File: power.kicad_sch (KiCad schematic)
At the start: 60 parts, among them U10 MAX4495AAUT, U11 MAX4495AAUT, U4 TPSM828302ARDSR, U5 LP3962EMP-3.3/NOPB, U6 STWD100NYWY3F, U7 MAX4495AAUT, U8 MP5073GG-P, U9 MAX4495AAUT

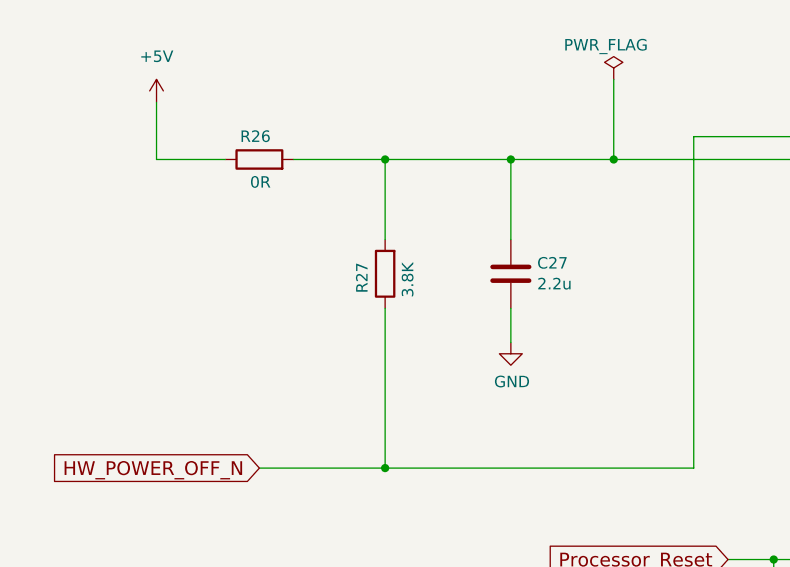
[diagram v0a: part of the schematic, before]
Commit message: Change a resistor, add a bunch of ground vias
Signed-off-by: Corey Minyard <corey@minyard.net>
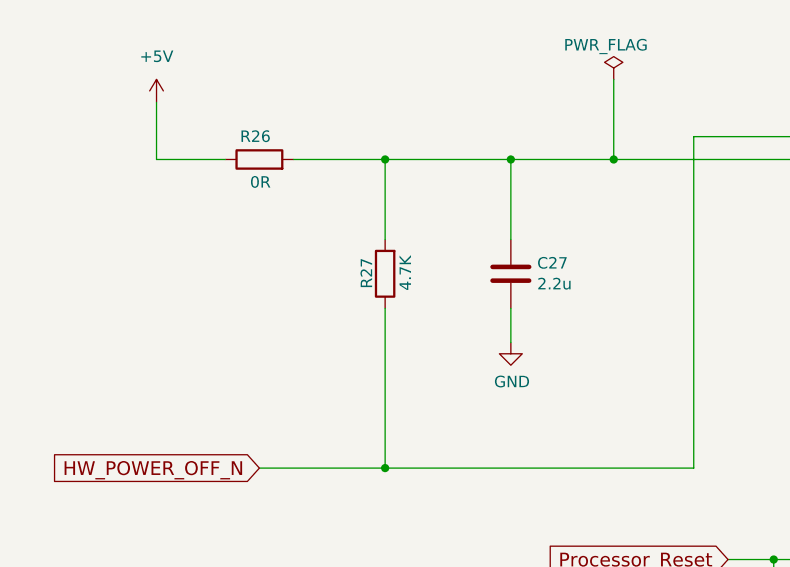
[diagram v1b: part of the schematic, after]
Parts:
- R27: value 3.8K -> 4.7K
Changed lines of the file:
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@@
 		(dnp no)
 		(property "Reference" "R27"
-			(at 63.5 104.14 90)
+			(at 64.008 103.632 90)
 			(effects
 				(font
@@
 			)
 		)
-		(property "Value" "3.8K"
-			(at 68.58 104.14 90)
+		(property "Value" "4.7K"
+			(at 68.326 103.378 90)
 			(effects
 				(font

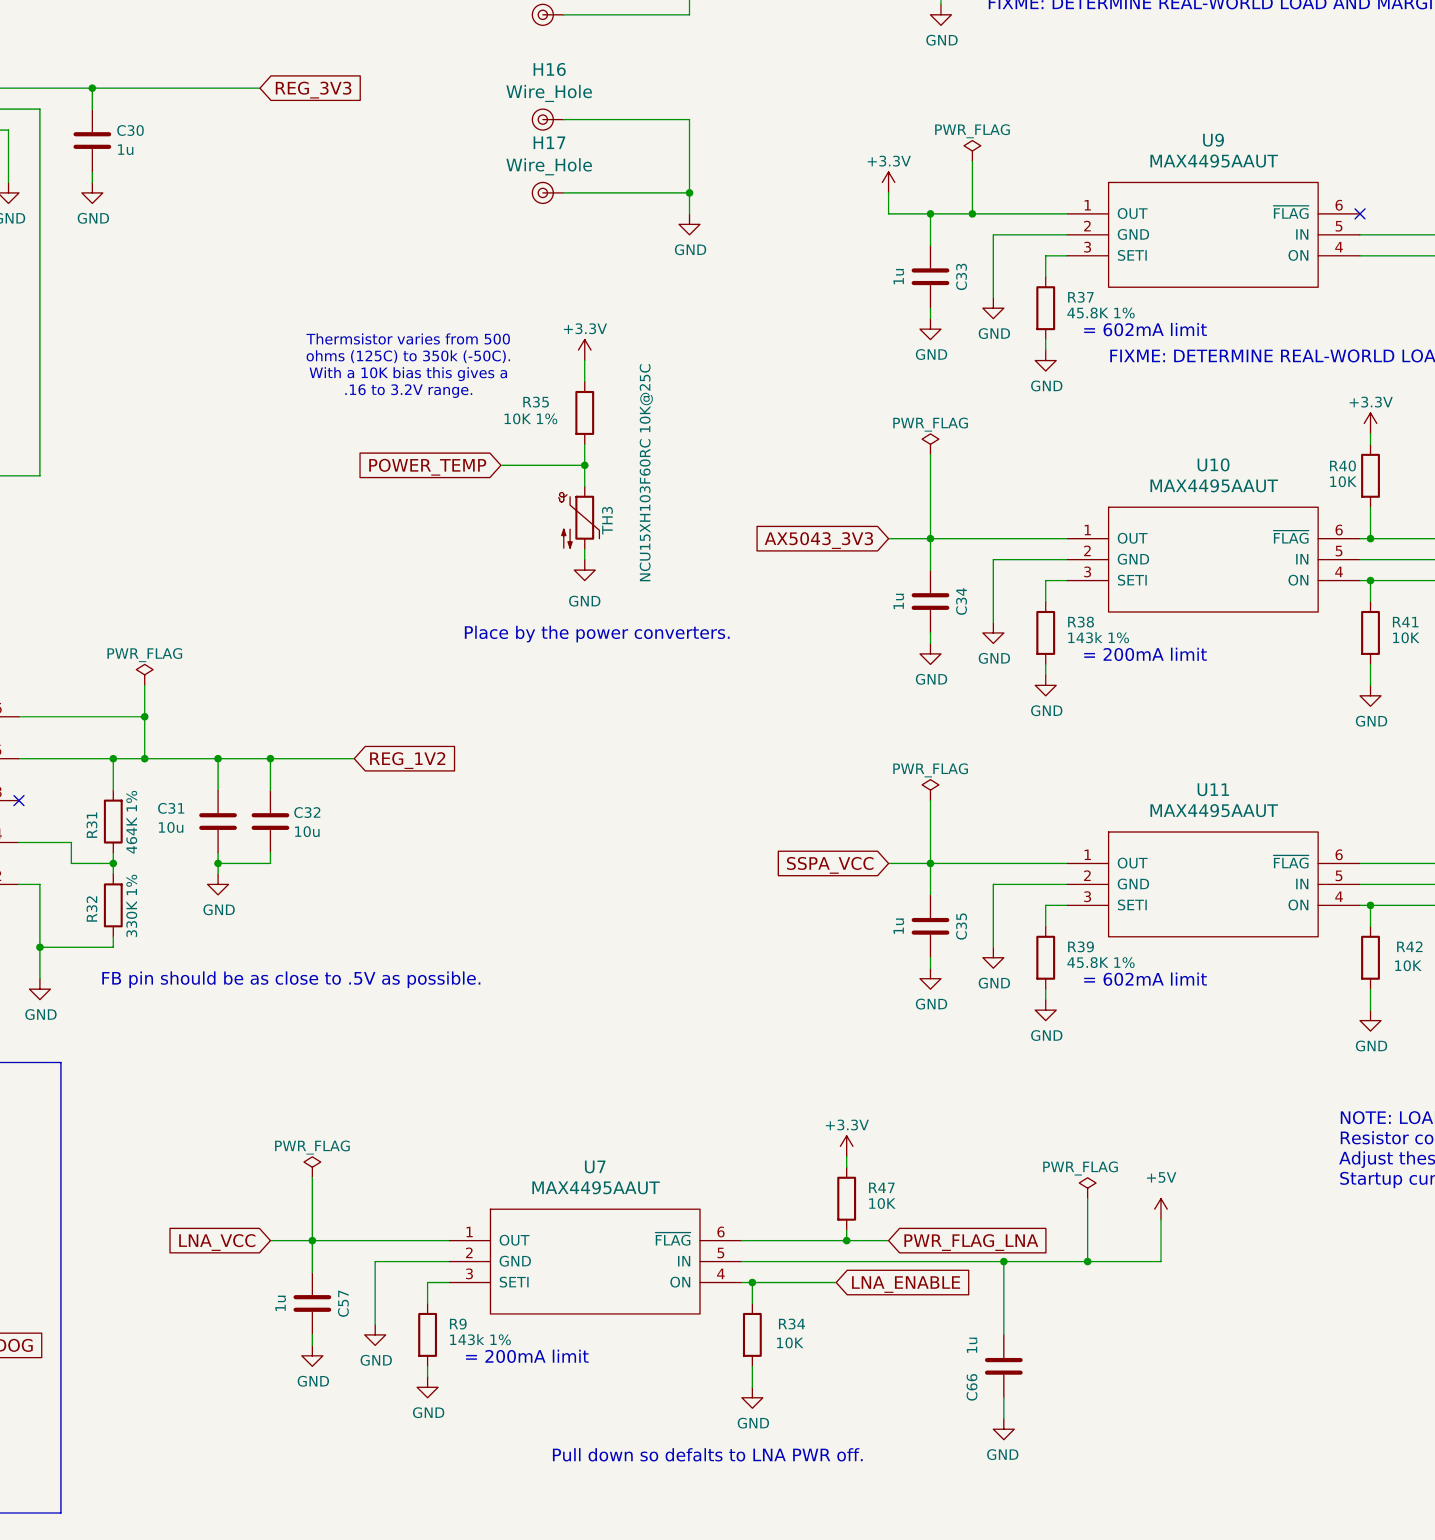
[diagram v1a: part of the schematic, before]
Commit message: Add a current limiter for on-board +5V devices
Signed-off-by: Corey Minyard <corey@minyard.net>
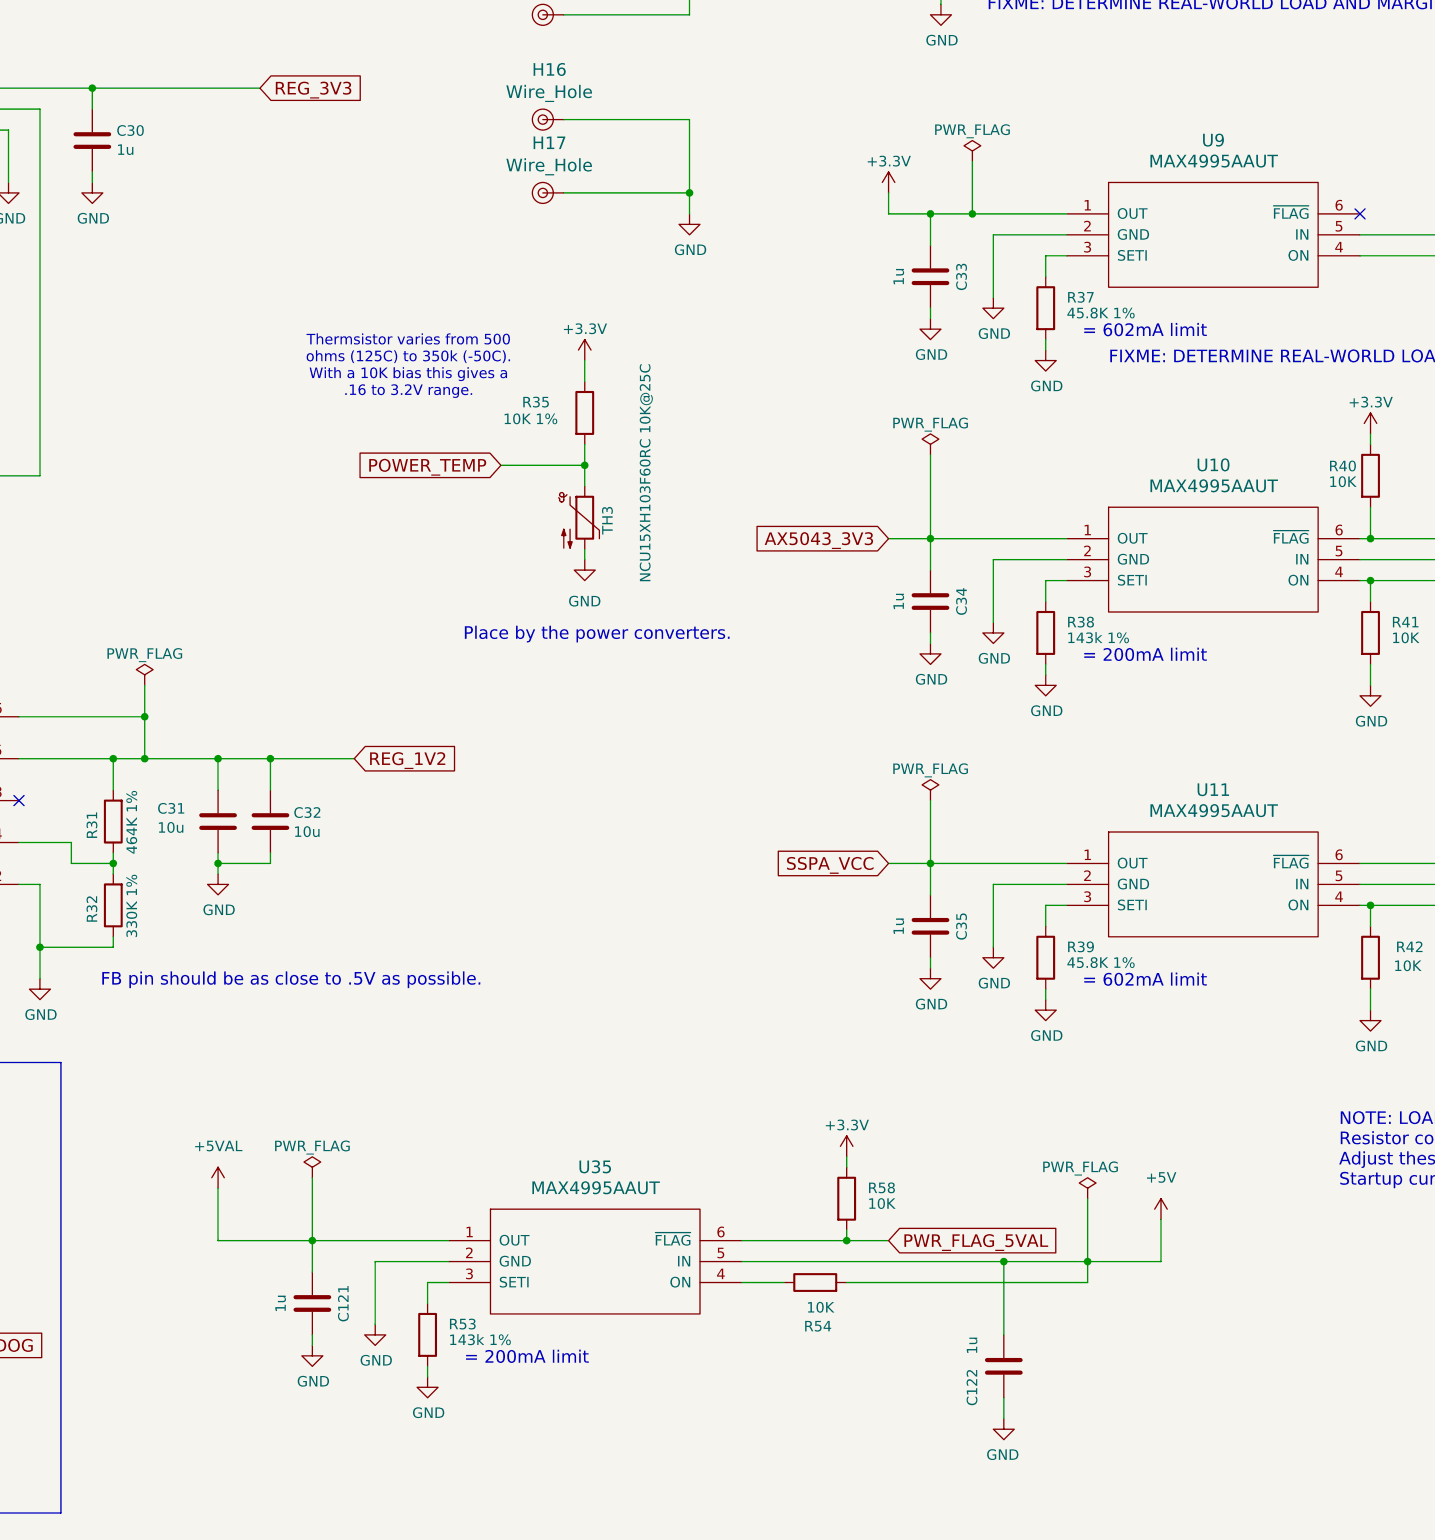
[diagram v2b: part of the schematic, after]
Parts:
- removed C57, C66: 1u, Capacitor_SMD:C_0805_2012Metric_Pad1.18x1.45mm_HandSolder, symbol Device:C
- removed R34, R47: 10K, Resistor_SMD:R_0603_1608Metric_Pad0.98x0.95mm_HandSolder, symbol Device:R
- removed R9: 143k 1%, Resistor_SMD:R_0603_1608Metric_Pad0.98x0.95mm_HandSolder, symbol Device:R
- removed U7: MAX4495AAUT, Package_TO_SOT_SMD:SOT-23-6_Handsoldering, symbol PACSAT_ICs:MAX4995AAUT
- added C121, C122: 1u, Capacitor_SMD:C_0805_2012Metric_Pad1.18x1.45mm_HandSolder, symbol Device:C
- added R53: 143k 1%, Resistor_SMD:R_0603_1608Metric_Pad0.98x0.95mm_HandSolder, symbol Device:R
- added R54, R58: 10K, Resistor_SMD:R_0603_1608Metric_Pad0.98x0.95mm_HandSolder, symbol Device:R
- added U35: MAX4995AAUT, Package_TO_SOT_SMD:SOT-23-6_Handsoldering, symbol PACSAT_ICs:MAX4995AAUT
- U10, U11, U9: value MAX4495AAUT -> MAX4995AAUT
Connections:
- net +3.3V: now also R58.1
- net +5V: now also C122.1, R54.2, U35.5 (IN)
- net GND: now also C121.2, C122.2, R53.2, U35.2 (GND)
- new net: R54.1, U35.4 (ON)
- new net: R53.1, U35.3 (SETI)
- new net +5VAL: C121.1, U35.1 (OUT)
- new net PWR_FLAG_5VAL: R58.2, U35.6 (~{FLAG})
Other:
- note removed: "Pull down so defalts to LNA PWR off."

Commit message: Add enable controls for the CAN bus transceivers
And do some more 0402 conversions.

Signed-off-by: Corey Minyard <corey@minyard.net>
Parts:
- C36: footprint Capacitor_SMD:C_0603_1608Metric_Pad1.08x0.95mm_HandSolder -> Capacitor_SMD:C_0402_1005Metric_Pad0.74x0.62mm_HandSolder
- R27, R28, R30, R31, R32, R35, R36, R37, R38, R39, R40, R41, R42, R43, R53, R58, R76: footprint Resistor_SMD:R_0603_1608Metric_Pad0.98x0.95mm_HandSolder -> Resistor_SMD:R_0402_1005Metric_Pad0.72x0.64mm_HandSolder
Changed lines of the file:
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@@
 			)
 		)
-		(property "Footprint" "Resistor_SMD:R_0603_1608Metric_Pad0.98x0.95mm_HandSolder"
+		(property "Footprint" "Resistor_SMD:R_0402_1005Metric_Pad0.72x0.64mm_HandSolder"
 			(at 285.242 156.21 90)
 			(effects
@@
 			)
 		)
-		(property "Footprint" "Resistor_SMD:R_0603_1608Metric_Pad0.98x0.95mm_HandSolder"
+		(property "Footprint" "Resistor_SMD:R_0402_1005Metric_Pad0.72x0.64mm_HandSolder"
 			(at 285.242 195.58 90)
 			(effects
@@
 			)
 		)
-		(property "Footprint" "Resistor_SMD:R_0603_1608Metric_Pad0.98x0.95mm_HandSolder"
+		(property "Footprint" "Resistor_SMD:R_0402_1005Metric_Pad0.72x0.64mm_HandSolder"
 			(at 285.242 116.84 90)
 			(effects
@@
 			)
 		)
-		(property "Footprint" "Resistor_SMD:R_0603_1608Metric_Pad0.98x0.95mm_HandSolder"
+		(property "Footprint" "Resistor_SMD:R_0402_1005Metric_Pad0.72x0.64mm_HandSolder"
 			(at 272.542 74.93 90)
 			(effects
@@
 			)
 		)
-		(property "Footprint" "Resistor_SMD:R_0603_1608Metric_Pad0.98x0.95mm_HandSolder"
+		(property "Footprint" "Resistor_SMD:R_0402_1005Metric_Pad0.72x0.64mm_HandSolder"
 			(at 82.042 228.6 90)
 			(effects
@@
 			)
 		)
-		(property "Footprint" "Resistor_SMD:R_0603_1608Metric_Pad0.98x0.95mm_HandSolder"
+		(property "Footprint" "Resistor_SMD:R_0402_1005Metric_Pad0.72x0.64mm_HandSolder"
 			(at 85.852 251.46 90)
 			(effects
@@
 			)
 		)
-		(property "Footprint" "Resistor_SMD:R_0603_1608Metric_Pad0.98x0.95mm_HandSolder"
+		(property "Footprint" "Resistor_SMD:R_0402_1005Metric_Pad0.72x0.64mm_HandSolder"
 			(at 324.612 156.21 90)
 			(effects
@@
 			)
 		)
-		(property "Footprint" "Resistor_SMD:R_0603_1608Metric_Pad0.98x0.95mm_HandSolder"
+		(property "Footprint" "Resistor_SMD:R_0402_1005Metric_Pad0.72x0.64mm_HandSolder"
 			(at 324.612 195.58 90)
 			(effects
@@
 			)
 		)
-		(property "Footprint" "Resistor_SMD:R_0603_1608Metric_Pad0.98x0.95mm_HandSolder"
+		(property "Footprint" "Resistor_SMD:R_0402_1005Metric_Pad0.72x0.64mm_HandSolder"
 			(at 67.818 105.41 90)
 			(effects
@@
 			)
 		)
-		(property "Footprint" "Resistor_SMD:R_0603_1608Metric_Pad0.98x0.95mm_HandSolder"
+		(property "Footprint" "Resistor_SMD:R_0402_1005Metric_Pad0.72x0.64mm_HandSolder"
 			(at 175.768 179.07 90)
 			(effects
@@
 			)
 		)
-		(property "Footprint" "Resistor_SMD:R_0603_1608Metric_Pad0.98x0.95mm_HandSolder"
+		(property "Footprint" "Resistor_SMD:R_0402_1005Metric_Pad0.72x0.64mm_HandSolder"
 			(at 229.362 129.54 90)
 			(effects
@@
 			)
 		)
-		(property "Footprint" "Resistor_SMD:R_0603_1608Metric_Pad0.98x0.95mm_HandSolder"
+		(property "Footprint" "Resistor_SMD:R_0402_1005Metric_Pad0.72x0.64mm_HandSolder"
 			(at 324.612 137.16 90)
 			(effects
@@
 			)
 		)
-		(property "Footprint" "Resistor_SMD:R_0603_1608Metric_Pad0.98x0.95mm_HandSolder"
+		(property "Footprint" "Resistor_SMD:R_0402_1005Metric_Pad0.72x0.64mm_HandSolder"
 			(at 95.25 236.728 90)
 			(effects
@@
 			)
 		)
-		(property "Footprint" "Resistor_SMD:R_0603_1608Metric_Pad0.98x0.95mm_HandSolder"
+		(property "Footprint" "Resistor_SMD:R_0402_1005Metric_Pad0.72x0.64mm_HandSolder"
 			(at 175.768 189.23 90)
 			(effects
@@
 			)
 		)
-		(property "Footprint" "Resistor_SMD:R_0603_1608Metric_Pad0.98x0.95mm_HandSolder"
+		(property "Footprint" "Resistor_SMD:R_0402_1005Metric_Pad0.72x0.64mm_HandSolder"
 			(at 261.112 224.79 90)
 			(effects
@@
 			)
 		)
-		(property "Footprint" "Resistor_SMD:R_0603_1608Metric_Pad0.98x0.95mm_HandSolder"
+		(property "Footprint" "Resistor_SMD:R_0402_1005Metric_Pad0.72x0.64mm_HandSolder"
 			(at 336.042 179.07 90)
 			(effects
@@
 			)
 		)
-		(property "Footprint" "Resistor_SMD:R_0603_1608Metric_Pad0.98x0.95mm_HandSolder"
+		(property "Footprint" "Resistor_SMD:R_0402_1005Metric_Pad0.72x0.64mm_HandSolder"
 			(at 210.312 241.3 90)
 			(effects
@@
 			)
 		)
-		(property "Footprint" "Capacitor_SMD:C_0603_1608Metric_Pad1.08x0.95mm_HandSolder"
+		(property "Footprint" "Capacitor_SMD:C_0402_1005Metric_Pad0.74x0.62mm_HandSolder"
 			(at 285.4452 63.5 0)
 			(effects
